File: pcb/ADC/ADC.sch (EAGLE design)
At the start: 11 parts, among them IC1 AD7997BRU, IC2 MCP1700

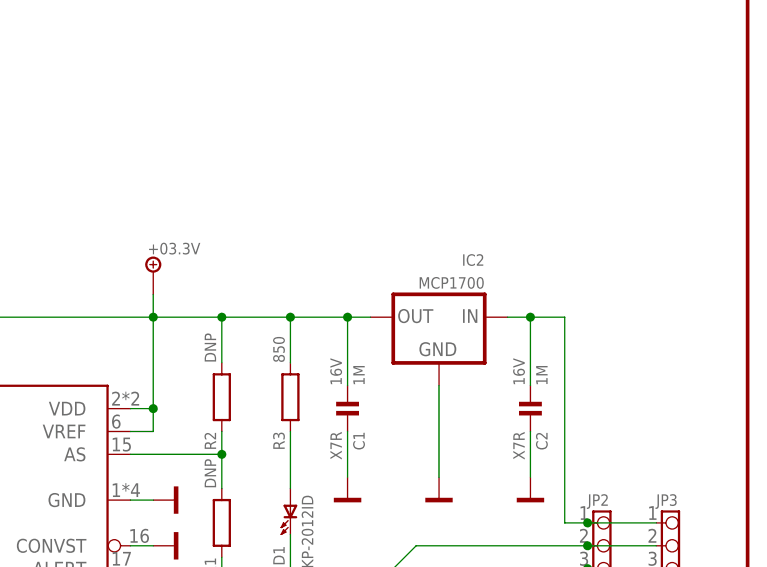
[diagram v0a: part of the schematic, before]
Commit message: Pridana dokumentace modulu ADC RevB
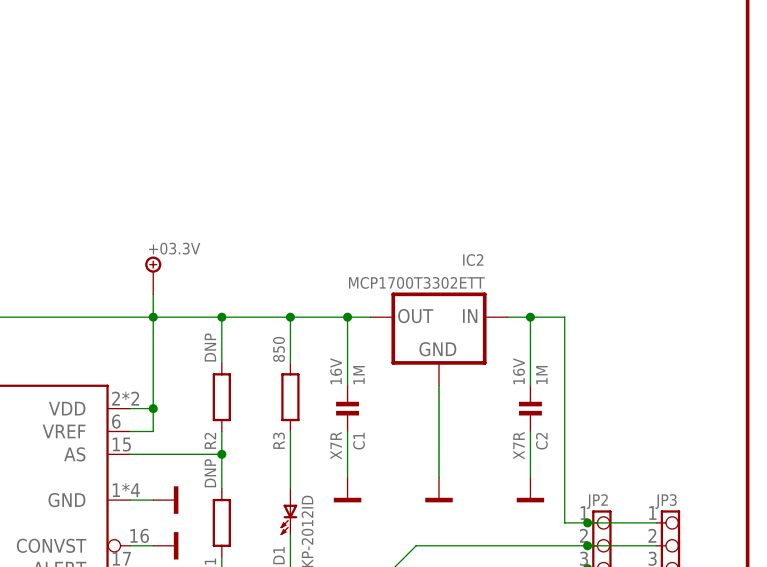
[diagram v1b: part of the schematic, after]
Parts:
- IC2: value MCP1700 -> MCP1700T3302ETT
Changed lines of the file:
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@@
 <part name="JP1" library="!pinhead" deviceset="PINHD-1X12" device="_254_EDGE" value="ZL201-12G"/>
 <part name="V10" library="!supply" deviceset="GND" device=""/>
-<part name="IC2" library="!stab" deviceset="MCP1700" device="" value="MCP1700"/>
+<part name="IC2" library="!stab" deviceset="MCP1700" device="" value="MCP1700T3302ETT"/>
 <part name="V11" library="!supply" deviceset="GND" device=""/>
 <part name="V12" library="!supply" deviceset="+03.3V" device=""/>

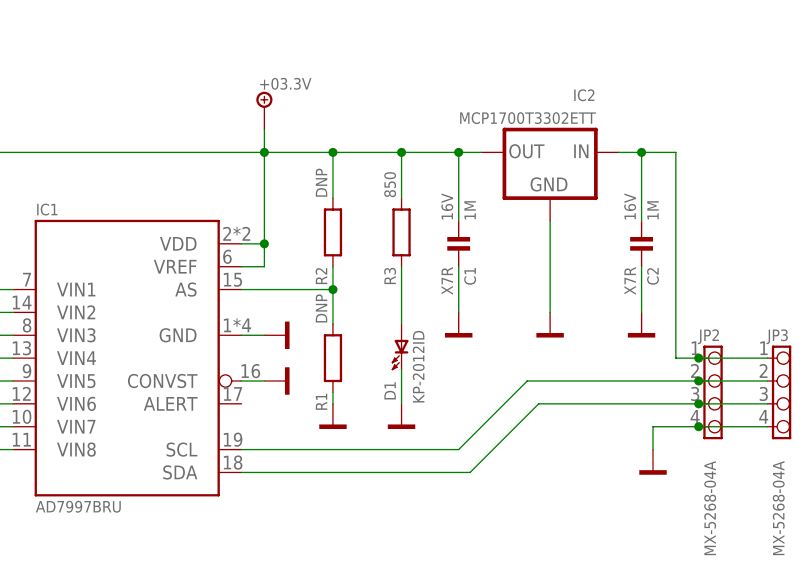
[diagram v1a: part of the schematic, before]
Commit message: Aktualizovany partlisty u obou modulu KM2 i ADC. Odkazy a ceny jsou uvnitr schematu.
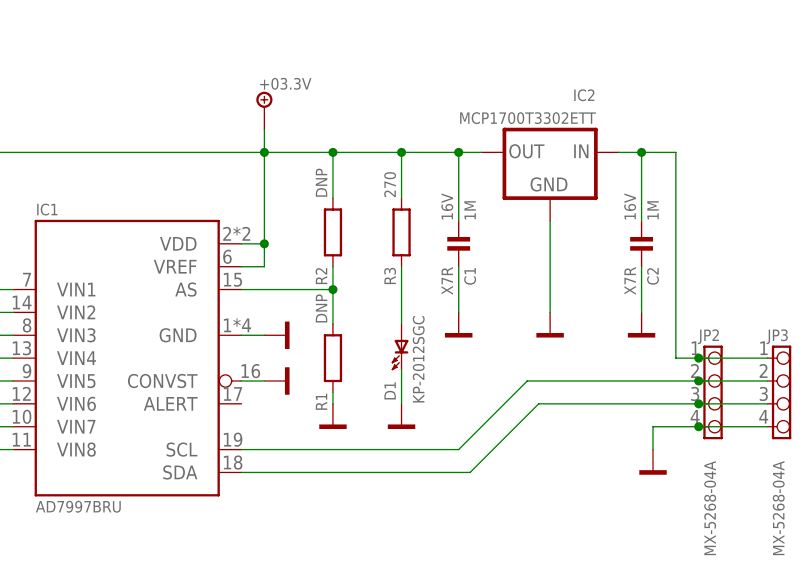
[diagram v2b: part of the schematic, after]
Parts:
- C1, C2: PRICE (none) -> 0.27; URL (none) -> http://www.tme.eu/cz/details/cl21b105kofnnng/kondenzatory-m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
- D1: value KP-2012ID -> KP-2012SGC; PRICE (none) -> 1.00; URL (none) -> http://www.tme.eu/cz/details/kp-2012sgc/diody-led-smd-barev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
- IC1: PRICE (none) -> 69.00; URL (none) -> https://www.gme.cz/ad7997bruz-0-tssop20-analog-devices
- IC2: PRICE (none) -> 8.78; URL (none) -> http://www.tme.eu/cz/details/mcp1700t3302ett/stabilizatory-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
- JP1: PRICE (none) -> 2.80; URL (none) -> http://www.tme.eu/cz/details/zl201-14g/konektory-hrebinky/c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
- JP2, JP3: PRICE (none) -> 2.52; URL (none) -> http://www.tme.eu/cz/details/mx-5268-04a/signalove-konektor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
- R3: value 850 -> 270; PRICE (none) -> 0.15; URL (none) -> http://www.tme.eu/cz/details/rc0805jr-07270r/rezistory-smd-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
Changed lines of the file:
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@@
 </classes>
 <parts>
-<part name="IC1" library="!ic_analogdevices" deviceset="AD7997" device="BRU"/>
-<part name="JP3" library="!pinhead" deviceset="PINHD-1X4" device="_250_MX5268" value="MX-5268-04A"/>
+<part name="IC1" library="!ic_analogdevices" deviceset="AD7997" device="BRU">
+<attribute name="PRICE" value="69.00"/>
+<attribute name="URL" value="https://www.gme.cz/ad7997bruz-0-tssop20-analog-devices"/>
+</part>
+<part name="JP3" library="!pinhead" deviceset="PINHD-1X4" device="_250_MX5268" value="MX-5268-04A">
+<attribute name="PRICE" value="2.52"/>
+<attribute name="URL" value="http://www.tme.eu/cz/details/mx-5268-04a/signalove-konektory-raster-250mm/molex/022057045-22-05-7045-5268-04a/"/>
+</part>
 <part name="V1" library="!supply" deviceset="GND" device=""/>
 <part name="V2" library="!supply" deviceset="GND" device=""/>
 <part name="V3" library="!supply" deviceset="GND" device=""/>
 <part name="C1" library="!discrete" deviceset="C" device="0805" value="1M">
+<attribute name="PRICE" value="0.27"/>
+<attribute name="URL" value="http://www.tme.eu/cz/details/cl21b105kofnnng/kondenzatory-mlcc-smd-0805/samsung/"/>
 <attribute name="VOLTAGE" value="16V"/>
 </part>
@@
 <part name="V5" library="!supply" deviceset="GND" device=""/>
 <part name="V8" library="!supply" deviceset="GND" device=""/>
-<part name="JP1" library="!pinhead" deviceset="PINHD-1X12" device="_254_EDGE" value="ZL201-12G"/>
+<part name="JP1" library="!pinhead" deviceset="PINHD-1X12" device="_254_EDGE" value="ZL201-12G">
+<attribute name="PRICE" value="2.80"/>
+<attribute name="URL" value="http://www.tme.eu/cz/details/zl201-14g/konektory-hrebinky/connfly/ds1021-1_14sf11/"/>
+</part>
 <part name="V10" library="!supply" deviceset="GND" device=""/>
-<part name="IC2" library="!stab" deviceset="MCP1700" device="" value="MCP1700T3302ETT"/>
+<part name="IC2" library="!stab" deviceset="MCP1700" device="" value="MCP1700T3302ETT">
+<attribute name="PRICE" value="8.78"/>
+<attribute name="URL" value="http://www.tme.eu/cz/details/mcp1700t3302ett/stabilizatory-napeti-neregulovane-ldo/microchip-technology/mcp1700t-3302ett/"/>
+</part>
 <part name="V11" library="!supply" deviceset="GND" device=""/>
 <part name="V12" library="!supply" deviceset="+03.3V" device=""/>
 <part name="C2" library="!discrete" deviceset="C" device="0805" value="1M">
+<attribute name="PRICE" value="0.27"/>
+<attribute name="URL" value="http://www.tme.eu/cz/details/cl21b105kofnnng/kondenzatory-mlcc-smd-0805/samsung/"/>
 <attribute name="VOLTAGE" value="16V"/>
 </part>
 <part name="V13" library="!supply" deviceset="GND" device=""/>
 <part name="V14" library="!supply" deviceset="GND" device=""/>
-<part name="JP2" library="!pinhead" deviceset="PINHD-1X4" device="_250_MX5268" value="MX-5268-04A"/>
-<part name="D1" library="!opto" deviceset="LED" device="0805" value="KP-2012ID"/>
-<part name="R3" library="!discrete" deviceset="R_" device="R0805" value="850"/>
+<part name="JP2" library="!pinhead" deviceset="PINHD-1X4" device="_250_MX5268" value="MX-5268-04A">
+<attribute name="PRICE" value="2.52"/>
+<attribute name="URL" value="http://www.tme.eu/cz/details/mx-5268-04a/signalove-konektory-raster-250mm/molex/022057045-22-05-7045-5268-04a/"/>
+</part>
+<part name="D1" library="!opto" deviceset="LED" device="0805" value="KP-2012SGC">
+<attribute name="PRICE" value="1.00"/>
+<attribute name="URL" value="http://www.tme.eu/cz/details/kp-2012sgc/diody-led-smd-barevne/kingbright-electronic/"/>
+</part>
+<part name="R3" library="!discrete" deviceset="R_" device="R0805" value="270">
+<attribute name="PRICE" value="0.15"/>
+<attribute name="URL" value="http://www.tme.eu/cz/details/rc0805jr-07270r/rezistory-smd-0805/yageo/rc0805jr-07270rl/"/>
+</part>
 <part name="V6" library="!supply" deviceset="GND" device=""/>
 <part name="U$1" library="!frames" deviceset="DIN_A5_" device=""/>
@@
 </plain>
 <instances>
-<instance part="IC1" gate="G$1" x="50.8" y="104.14"/>
+<instance part="IC1" gate="G$1" x="50.8" y="104.14">
+<attribute name="PRICE" x="50.8" y="104.14" size="1.778" layer="96" display="off"/>
+<attribute name="URL" x="50.8" y="104.14" size="1.778" layer="96" display="off"/>
+</instance>
 <instance part="JP3" gate="A" x="124.46" y="99.06" smashed="yes">
 <attribute name="NAME" x="121.92" y="106.68" size="1.27" layer="95" align="center-left"/>
 <attribute name="VALUE" x="123.19" y="92.71" size="1.27" layer="96" rot="R270" align="center-left"/>
+<attribute name="PRICE" x="124.46" y="99.06" size="1.778" layer="96" display="off"/>
+<attribute name="URL" x="124.46" y="99.06" size="1.778" layer="96" display="off"/>
 </instance>
 <instance part="V1" gate="GND" x="15.24" y="101.6" rot="R90"/>
 <instance part="V2" gate="GND" x="15.24" y="104.14" rot="R90"/>
 <instance part="V3" gate="GND" x="68.58" y="106.68" rot="R90"/>
-<instance part="C1" gate="G$1" x="87.63" y="116.84" rot="R270"/>
+<instance part="C1" gate="G$1" x="87.63" y="116.84" rot="R270">
+<attribute name="PRICE" x="87.63" y="116.84" size="1.778" layer="96" display="off"/>
+<attribute name="URL" x="87.63" y="116.84" size="1.778" layer="96" display="off"/>
+</instance>
 <instance part="V4" gate="GND" x="87.63" y="106.68"/>
 <instance part="R1" gate="G$1" x="73.66" y="102.87" smashed="yes" rot="R270">
@@
 </instance>
 <instance part="V8" gate="GND" x="109.22" y="91.44"/>
-<instance part="JP1" gate="G$1" x="7.62" y="101.6" rot="R180"/>
+<instance part="JP1" gate="G$1" x="7.62" y="101.6" rot="R180">
+<attribute name="PRICE" x="7.62" y="101.6" size="1.778" layer="96" display="off"/>
+<attribute name="URL" x="7.62" y="101.6" size="1.778" layer="96" display="off"/>
+</instance>
 <instance part="V10" gate="GND" x="15.24" y="88.9" rot="R90"/>
-<instance part="IC2" gate="G$1" x="97.79" y="127" rot="MR0"/>
+<instance part="IC2" gate="G$1" x="97.79" y="127" rot="MR0">
+<attribute name="PRICE" x="97.79" y="127" size="1.778" layer="96" display="off"/>
+<attribute name="URL" x="97.79" y="127" size="1.778" layer="96" display="off"/>
+</instance>
 <instance part="V11" gate="GND" x="97.79" y="106.68"/>
 <instance part="V12" gate="G$1" x="66.04" y="132.08"/>
-<instance part="C2" gate="G$1" x="107.95" y="116.84" rot="R270"/>
+<instance part="C2" gate="G$1" x="107.95" y="116.84" rot="R270">
+<attribute name="PRICE" x="107.95" y="116.84" size="1.778" layer="96" display="off"/>
+<attribute name="URL" x="107.95" y="116.84" size="1.778" layer="96" display="off"/>
+</instance>
 <instance part="V13" gate="GND" x="107.95" y="106.68"/>
 <instance part="V14" gate="GND" x="68.58" y="101.6" rot="R90"/>
@@
 <attribute name="NAME" x="114.3" y="106.68" size="1.27" layer="95" align="center-left"/>
 <attribute name="VALUE" x="115.57" y="92.71" size="1.27" layer="96" rot="R270" align="center-left"/>
+<attribute name="PRICE" x="116.84" y="99.06" size="1.778" layer="96" display="off"/>
+<attribute name="URL" x="116.84" y="99.06" size="1.778" layer="96" display="off"/>
 </instance>
 <instance part="D1" gate="G$1" x="81.28" y="105.41" smashed="yes">
 <attribute name="NAME" x="79.375" y="101.6" size="1.27" layer="95" rot="R270"/>
 <attribute name="VALUE" x="83.82" y="99.06" size="1.27" layer="96" rot="R90"/>
+<attribute name="PRICE" x="81.28" y="105.41" size="1.778" layer="96" display="off"/>
+<attribute name="URL" x="81.28" y="105.41" size="1.778" layer="96" display="off"/>
 </instance>
 <instance part="R3" gate="G$1" x="81.28" y="119.38" smashed="yes" rot="R90">
@@
 <attribute name="VALUE" x="80.01" y="121.92" size="1.27" layer="96" rot="R90" align="center-left"/>
 <attribute name="TOLERANCE" x="81.28" y="120.65" size="1.27" layer="96" rot="R270" align="center-left"/>
+<attribute name="PRICE" x="81.28" y="119.38" size="1.778" layer="96" display="off"/>
+<attribute name="URL" x="81.28" y="119.38" size="1.778" layer="96" display="off"/>
 </instance>
 <instance part="V6" gate="GND" x="81.28" y="96.52" smashed="yes">
